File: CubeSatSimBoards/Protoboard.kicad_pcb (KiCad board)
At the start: 2 copper layers, 857 parts, among them J1 Conn_02x20_Odd_Even

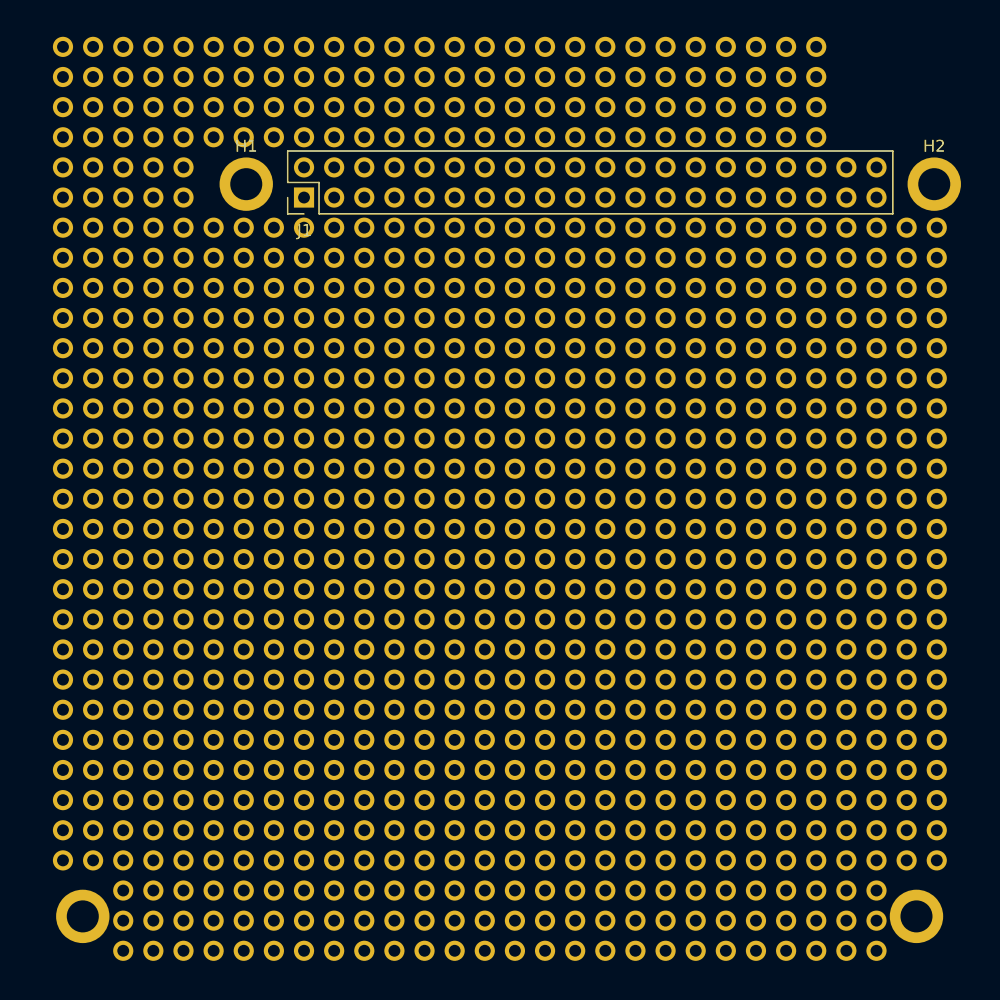
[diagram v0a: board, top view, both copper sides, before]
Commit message: Fixed outline problem on Empty board and Protoboard
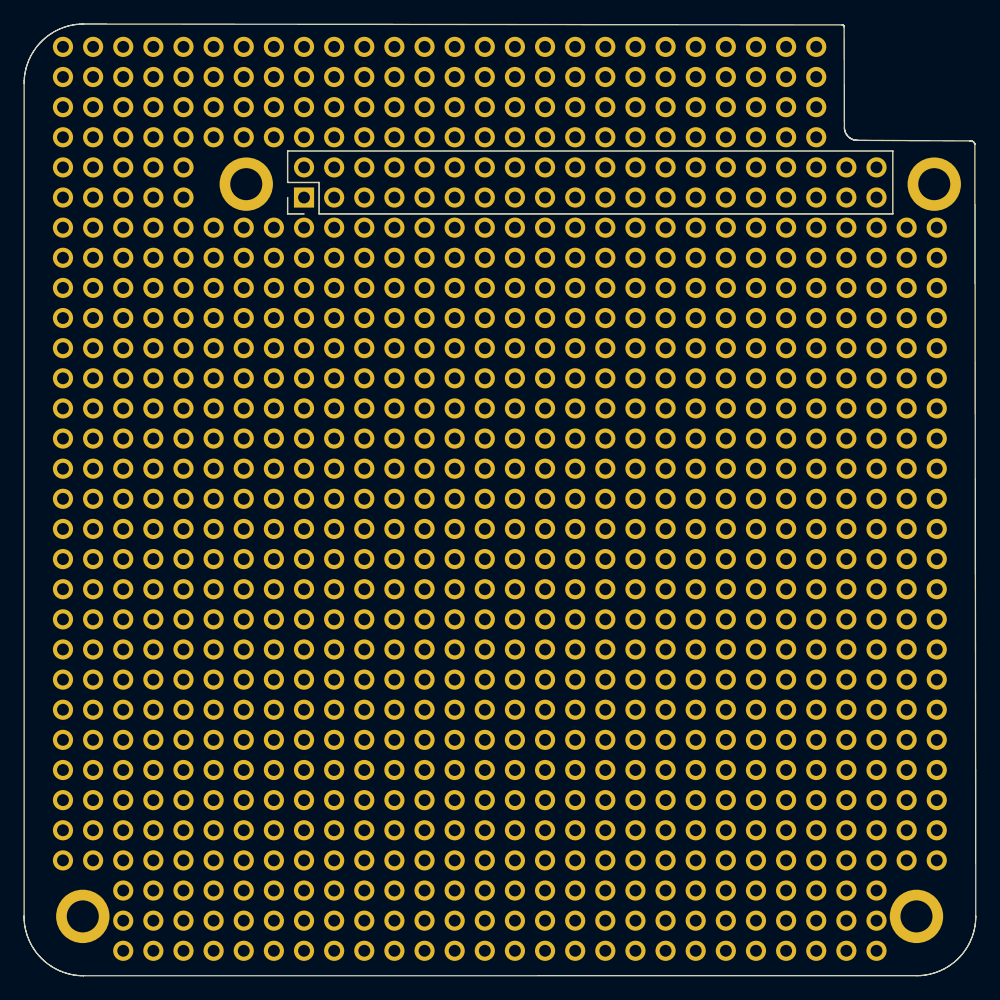
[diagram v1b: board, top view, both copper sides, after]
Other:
- board outline added: 80.2 x 80.2 mm

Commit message: Added cutouts, brokenout Pi header pins and label to protoboard
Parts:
- removed the ? at (107.4, 106.2)
- removed the ? at (148.1, 162.1)
- removed the ? at (150.6, 159.5)
- removed the ? at (137.9, 93.5)
- removed the ? at (145.5, 103.7)
- removed the ? at (84.5, 157.0)
- removed the ? at (84.5, 154.5)
- removed the ? at (135.3, 96.0)
- removed the ? at (122.7, 93.5)
- removed the ? at (125.2, 103.7)
- removed the ? at (120.1, 93.5)
- removed the ? at (132.8, 103.7)
- removed the ? at (145.5, 162.1)
- removed the ? at (145.5, 164.6)
- removed the ? at (130.3, 93.5)
- removed the ? at (127.7, 103.7)
- removed the ? at (104.9, 106.2)
- removed the ? at (140.4, 96.0)
- removed the ? at (110.0, 93.5)
- removed the ? at (87.1, 151.9)
- removed the ? at (145.5, 159.5)
- removed the ? at (143.0, 106.2)
- removed the ? at (148.1, 93.5)
- removed the ? at (145.5, 93.5)
- removed the ? at (132.8, 93.5)
- removed the ? at (137.9, 106.2)
- removed the ? at (104.9, 103.7)
- removed the ? at (104.9, 96.0)
- removed the ? at (145.5, 96.0)
- removed the ? at (117.6, 103.7)
- removed the ? at (120.1, 106.2)
- removed the ? at (130.3, 103.7)
- removed the ? at (117.6, 96.0)
- removed the ? at (125.2, 93.5)
- removed the ? at (112.5, 96.0)
- removed the ? at (110.0, 103.7)
- removed the ? at (135.3, 106.2)
- removed the ? at (153.1, 164.6)
- removed the ? at (137.9, 96.0)
- removed the ? at (115.0, 103.7)
- removed the ? at (148.1, 96.0)
- removed the ? at (130.3, 96.0)
- removed the ? at (132.8, 106.2)
- removed the ? at (125.2, 96.0)
- removed the ? at (115.0, 93.5)
- removed the ? at (125.2, 106.2)
- removed the ? at (112.5, 106.2)
- removed the ? at (122.7, 96.0)
- removed the ? at (110.0, 106.2)
- removed the ? at (120.1, 96.0)
- removed the ? at (150.6, 106.2)
- removed the ? at (110.0, 96.0)
- removed the ? at (143.0, 96.0)
- removed the ? at (84.5, 149.4)
- removed the ? at (148.1, 103.7)
- removed the ? at (148.1, 106.2)
- removed the ? at (112.5, 93.5)
- removed the ? at (127.7, 96.0)
- removed the ? at (87.1, 154.5)
- removed the ? at (153.1, 106.2)
- removed the ? at (115.0, 106.2)
- removed the ? at (120.1, 103.7)
- removed the ? at (153.1, 103.7)
- removed the ? at (150.6, 162.1)
- removed the ? at (140.4, 93.5)
- removed the ? at (117.6, 93.5)
- removed the ? at (107.4, 103.7)
- removed the ? at (127.7, 106.2)
- removed the ? at (148.1, 159.5)
- removed the ? at (143.0, 164.6)
- removed the ? at (145.5, 106.2)
- removed the ? at (140.4, 106.2)
- removed the ? at (132.8, 96.0)
- removed the ? at (87.1, 149.4)
- removed the ? at (115.0, 96.0)
- removed the ? at (143.0, 103.7)
- removed the ? at (104.9, 93.5)
- removed the ? at (122.7, 106.2)
- removed the ? at (84.5, 151.9)
- removed the ? at (150.6, 103.7)
- removed the ? at (107.4, 93.5)
- removed the ? at (150.6, 164.6)
- removed the ? at (130.3, 106.2)
- removed the ? at (122.7, 103.7)
- removed the ? at (127.7, 93.5)
- removed the ? at (143.0, 93.5)
- removed the ? at (137.9, 103.7)
- removed the ? at (143.0, 159.5)
- removed the ? at (117.6, 106.2)
- removed the ? at (135.3, 103.7)
- removed the ? at (140.4, 103.7)
- removed the ? at (107.4, 96.0)
- removed the ? at (143.0, 162.1)
- removed the ? at (148.1, 164.6)
- removed the ? at (153.1, 159.5)
- removed the ? at (112.5, 103.7)
- removed the ? at (153.1, 162.1)
- removed the ? at (135.3, 93.5)
- added J2: Conn_01x20_Pin, Connector_PinHeader_2.54mm:PinHeader_1x20_P2.54mm_Vertical, F.Cu at (104.9, 103.7)
- added J3: Conn_01x20_Pin, Connector_PinHeader_2.54mm:PinHeader_1x20_P2.54mm_Vertical, F.Cu at (104.9, 96.0)
- added J4: Conn_01x20_Pin, Connector_PinHeader_2.54mm:PinHeader_1x20_P2.54mm_Vertical, F.Cu at (104.9, 93.5)
- added J5: Conn_01x20_Pin, Connector_PinHeader_2.54mm:PinHeader_1x20_P2.54mm_Vertical, F.Cu at (104.9, 106.2)
- moved ? 8.03 mm to (87.1, 149.4)
- moved ? 8.03 mm to (87.1, 151.9)
- moved ? 8.03 mm to (87.1, 154.5)
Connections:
- J1 pad 1: unconnected-(J1-Pin_1-Pad1) -> Net-(J1-Pin_1)
- J1 pad 10: unconnected-(J1-Pin_10-Pad10) -> Net-(J1-Pin_10)
- J1 pad 11: unconnected-(J1-Pin_11-Pad11) -> Net-(J1-Pin_11)
- J1 pad 12: unconnected-(J1-Pin_12-Pad12) -> Net-(J1-Pin_12)
- J1 pad 13: unconnected-(J1-Pin_13-Pad13) -> Net-(J1-Pin_13)
- J1 pad 14: unconnected-(J1-Pin_14-Pad14) -> Net-(J1-Pin_14)
- J1 pad 15: unconnected-(J1-Pin_15-Pad15) -> Net-(J1-Pin_15)
- J1 pad 16: unconnected-(J1-Pin_16-Pad16) -> Net-(J1-Pin_16)
- J1 pad 17: unconnected-(J1-Pin_17-Pad17) -> Net-(J1-Pin_17)
- J1 pad 18: unconnected-(J1-Pin_18-Pad18) -> Net-(J1-Pin_18)
- J1 pad 19: unconnected-(J1-Pin_19-Pad19) -> Net-(J1-Pin_19)
- J1 pad 2: unconnected-(J1-Pin_2-Pad2) -> Net-(J1-Pin_2)
- J1 pad 20: unconnected-(J1-Pin_20-Pad20) -> Net-(J1-Pin_20)
- J1 pad 21: unconnected-(J1-Pin_21-Pad21) -> Net-(J1-Pin_21)
- J1 pad 22: unconnected-(J1-Pin_22-Pad22) -> Net-(J1-Pin_22)
- J1 pad 23: unconnected-(J1-Pin_23-Pad23) -> Net-(J1-Pin_23)
- J1 pad 24: unconnected-(J1-Pin_24-Pad24) -> Net-(J1-Pin_24)
- J1 pad 25: unconnected-(J1-Pin_25-Pad25) -> Net-(J1-Pin_25)
- J1 pad 26: unconnected-(J1-Pin_26-Pad26) -> Net-(J1-Pin_26)
- J1 pad 27: unconnected-(J1-Pin_27-Pad27) -> Net-(J1-Pin_27)
- J1 pad 28: unconnected-(J1-Pin_28-Pad28) -> Net-(J1-Pin_28)
- J1 pad 29: unconnected-(J1-Pin_29-Pad29) -> Net-(J1-Pin_29)
- J1 pad 3: unconnected-(J1-Pin_3-Pad3) -> Net-(J1-Pin_3)
- J1 pad 30: unconnected-(J1-Pin_30-Pad30) -> Net-(J1-Pin_30)
- J1 pad 31: unconnected-(J1-Pin_31-Pad31) -> Net-(J1-Pin_31)
- J1 pad 32: unconnected-(J1-Pin_32-Pad32) -> Net-(J1-Pin_32)
- J1 pad 33: unconnected-(J1-Pin_33-Pad33) -> Net-(J1-Pin_33)
- J1 pad 34: unconnected-(J1-Pin_34-Pad34) -> Net-(J1-Pin_34)
- J1 pad 35: unconnected-(J1-Pin_35-Pad35) -> Net-(J1-Pin_35)
- J1 pad 36: unconnected-(J1-Pin_36-Pad36) -> Net-(J1-Pin_36)
- J1 pad 37: unconnected-(J1-Pin_37-Pad37) -> Net-(J1-Pin_37)
- J1 pad 38: unconnected-(J1-Pin_38-Pad38) -> Net-(J1-Pin_38)
- J1 pad 39: unconnected-(J1-Pin_39-Pad39) -> Net-(J1-Pin_39)
- J1 pad 4: unconnected-(J1-Pin_4-Pad4) -> Net-(J1-Pin_4)
- J1 pad 40: unconnected-(J1-Pin_40-Pad40) -> Net-(J1-Pin_40)
- J1 pad 5: unconnected-(J1-Pin_5-Pad5) -> Net-(J1-Pin_5)
- J1 pad 6: unconnected-(J1-Pin_6-Pad6) -> Net-(J1-Pin_6)
- J1 pad 7: unconnected-(J1-Pin_7-Pad7) -> Net-(J1-Pin_7)
- J1 pad 8: unconnected-(J1-Pin_8-Pad8) -> Net-(J1-Pin_8)
- J1 pad 9: unconnected-(J1-Pin_9-Pad9) -> Net-(J1-Pin_9)
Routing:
- net Net-(J1-Pin_9): track 0.00 -> 10.2 mm
- net Net-(J1-Pin_8): track 0.00 -> 10.2 mm
- net Net-(J1-Pin_7): track 0.00 -> 10.2 mm
- net Net-(J1-Pin_6): track 0.00 -> 10.2 mm
- net Net-(J1-Pin_5): track 0.00 -> 10.2 mm
- net Net-(J1-Pin_40): track 0.00 -> 10.2 mm
- net Net-(J1-Pin_4): track 0.00 -> 10.2 mm
- net Net-(J1-Pin_39): track 0.00 -> 10.2 mm
- net Net-(J1-Pin_38): track 0.00 -> 10.2 mm
- net Net-(J1-Pin_37): track 0.00 -> 10.2 mm
- net Net-(J1-Pin_36): track 0.00 -> 10.2 mm
- net Net-(J1-Pin_35): track 0.00 -> 10.2 mm
- net Net-(J1-Pin_34): track 0.00 -> 10.2 mm
- net Net-(J1-Pin_33): track 0.00 -> 10.2 mm
- net Net-(J1-Pin_32): track 0.00 -> 10.2 mm
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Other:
- board size 80.2 x 80.2 mm -> 80.2 x 80.3 mm
- board text added: "Pioneer CubeSat Club 2026 Protoboard V1"
